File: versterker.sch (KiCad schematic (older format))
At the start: 0 parts

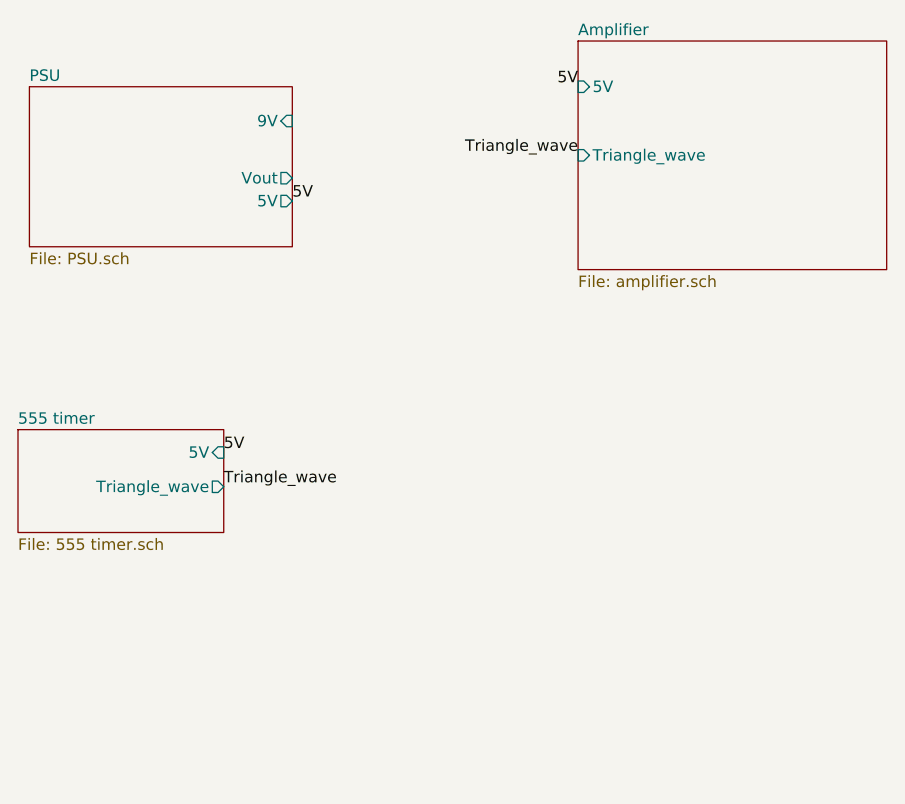
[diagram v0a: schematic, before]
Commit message: added filter end stage
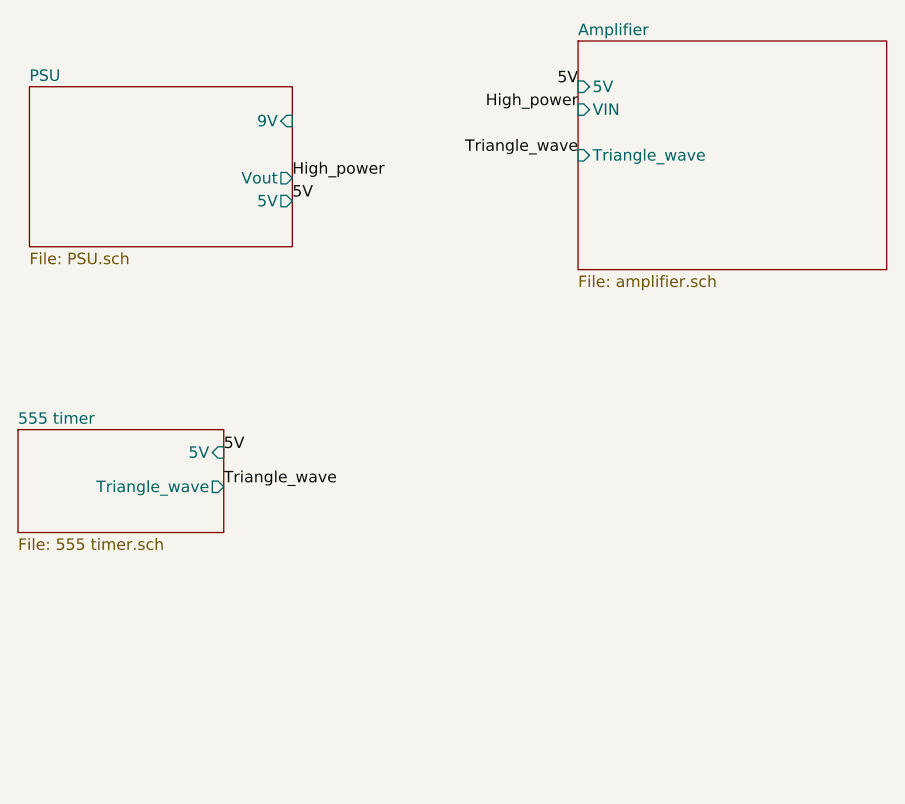
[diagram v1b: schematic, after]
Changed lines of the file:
@@
 F2 "5V" I L 3950 1600 50
 F3 "Triangle_wave" I L 3950 1900 50
+F4 "VIN" I L 3950 1700 50
 $EndSheet
 $Sheet
@@
 Text Label 3950 1600 2    50   ~ 0
 5V
+Text Label 2700 2000 0    50   ~ 0
+High_power
+Text Label 3950 1700 2    50   ~ 0
+High_power
 $EndSCHEMATC

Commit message: created pcb
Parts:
- added D1: D_SMCJ9.0CA_TVS, MAIN_PCB_LIB:D_9V_TVS_SMCJ-Q, symbol Main_Library:D_SMCJ9.0CA_TVS
- added D2: D_RED_0603_Wurth_150060RS75000, MAIN_PCB_LIB:D_RED_0603_Wurth, symbol Main_Library:D_RED_0603_Wurth_150060RS75000
- added J1: J_Barreljack_3.5mm_Wurth_TH, MAIN_PCB_LIB:J_Barreljack_3.5mm_Wurth, symbol Main_Library:J_Barreljack_3.5mm_Wurth_TH
- added R1: R_10K_0603, MAIN_PCB_LIB:R_0603, symbol Main_Library:R_10K_0603
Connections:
- new net: D2.1 (CATHODE), R1.1
- new net 9V: D1.1, D2.2 (ANODE), J1.1
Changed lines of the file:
@@
 $Descr A4 11693 8268
 encoding utf-8
-Sheet 1 4
+Sheet 1 5
 Title ""
 Date ""
@@
 $EndDescr
 $Sheet
-S 1550 1600 1150 700
+S 2150 1600 550  600
 U 615215B7
 F0 "PSU" 50
@@
 $EndSheet
 $Sheet
-S 3950 1400 1350 1000
+S 3950 1400 750  750
 U 6152C63E
 F0 "Amplifier" 50
@@
 $EndSheet
 $Sheet
-S 1500 3100 900  450
+S 2150 2550 900  450
 U 6158BEDE
 F0 "555 timer" 50
 F1 "555 timer.sch" 50
-F2 "5V" I R 2400 3200 50
-F3 "Triangle_wave" O R 2400 3350 50
+F2 "5V" I R 3050 2650 50
+F3 "Triangle_wave" O R 3050 2800 50
 $EndSheet
-Text Label 2400 3350 0    50   ~ 0
+Text Label 3050 2800 0    50   ~ 0
 Triangle_wave
 Text Label 3950 1900 2    50   ~ 0
@@
 Text Label 2700 2100 0    50   ~ 0
 5V
-Text Label 2400 3200 0    50   ~ 0
+Text Label 3050 2650 0    50   ~ 0
 5V
 Text Label 3950 1600 2    50   ~ 0
@@
 Text Label 3950 1700 2    50   ~ 0
 High_power
+$Sheet
+S 4100 2650 650  450
+U 616ED187
+F0 "VU-Meter" 50
+F1 "VU-Meter.sch" 50
+F2 "9V" I L 4100 2800 50
+F3 "Signal" I L 4100 2950 50
+$EndSheet
+Text Label 2700 1750 0    50   ~ 0
+9V
+Text Label 4100 2800 2    50   ~ 0
+9V
+Text Label 4100 2950 2    50   ~ 0
+High_power
+$Comp
+L Main_Library:J_Barreljack_3.5mm_Wurth_TH J1
+U 1 1 6176EC14
+P 2750 3750
+F 0 "J1" H 2570 3898 50  0000 C CNN
+F 1 "J_Barreljack_3.5mm_Wurth_TH" H 2350 3450 50  0001 L BNN
+F 2 "MAIN_PCB_LIB:J_Barreljack_3.5mm_Wurth" H 2750 3750 50  0001 L BNN
+F 3 "" H 2750 3750 50  0001 L BNN
+F 4 "710-694102303002" H 2750 3750 50  0001 C CNN "Mouser"
+	1    2750 3750
+	1    0    0    -1
+$EndComp
+Text Label 3500 3750 0    50   ~ 0
+9V
+$Comp
+L Main_Library:GND #GND01
+U 1 1 6177185F
+P 2900 3950
+F 0 "#GND01" H 2740 3930 50  0001 C CNN
+F 1 "GND" H 2740 3930 50  0001 C CNN
+F 2 "" H 2810 3890 50  0001 C CNN
+F 3 "" H 2810 3890 50  0001 C CNN
+	1    2900 3950
+	1    0    0    -1
+$EndComp
+Wire Wire Line
+	2750 3850 2900 3850
+Wire Wire Line
+	2900 3850 2900 3950
+$Comp
+L Main_Library:D_SMCJ9.0CA_TVS D1
+U 1 1 61776F94
+P 3100 4050
+F 0 "D1" V 3050 4130 50  0000 L CNN
+F 1 "D_SMCJ9.0CA_TVS" H 2800 3855 50  0001 L BNN
+F 2 "MAIN_PCB_LIB:D_9V_TVS_SMCJ-Q" H 3100 4050 50  0001 L BNN
+F 3 "" H 3100 4050 50  0001 L BNN
+F 4 "IPC-7351B" H 3100 4050 50  0001 L BNN "STANDARD"
+F 5 "Diodes Incorporated" H 3100 4050 50  0001 L BNN "MANUFACTURER"
+F 6 "2.62mm" H 3100 4050 50  0001 L BNN "MAXIMUM_PACKAGE_HEIGHT"
+F 7 "11/20/15" H 3100 4050 50  0001 L BNN "PARTREV"
+F 8 "576-SMCJ9.0CA" H 3100 4050 50  0001 C CNN "Mouser"
+	1    3100 4050
+	0    1    1    0
+$EndComp
+$Comp
+L Main_Library:GND #GND02
+U 1 1 617783BE
+P 3100 4250
+F 0 "#GND02" H 2940 4230 50  0001 C CNN
+F 1 "GND" H 2940 4230 50  0001 C CNN
+F 2 "" H 3010 4190 50  0001 C CNN
+F 3 "" H 3010 4190 50  0001 C CNN
+	1    3100 4250
+	1    0    0    -1
+$EndComp
+$Comp
+L Main_Library:D_RED_0603_Wurth_150060RS75000 D2
+U 1 1 617794CD
+P 3500 3700
+F 0 "D2" V 3846 3572 50  0000 R CNN
+F 1 "D_RED_0603_Wurth_150060RS75000" H 3500 4200 50  0001 L CNN
+F 2 "MAIN_PCB_LIB:D_RED_0603_Wurth" H 3500 4300 50  0001 L CNN
+F 3 "https://www.we-online.com/catalog/datasheet/150060RS75000.pdf" H 3500 4400 50  0001 L CNN
+F 4 "No" H 3500 4500 50  0001 L CNN "automotive"
+F 5 "Diode" H 3500 4600 50  0001 L CNN "category"
+F 6 "Red" V 3755 3572 50  0000 R CNN "colour"
+F 7 "Optoelectronics" H 3500 4800 50  0001 L CNN "device class L1"
+F 8 "LEDs" H 3500 4900 50  0001 L CNN "device class L2"
+F 9 "unset" H 3500 5000 50  0001 L CNN "device class L3"
+F 10 "LED RED CLEAR 0603 SMD" H 3500 5100 50  0001 L CNN "digikey description"
+F 11 "732-4978-1-ND" H 3500 5200 50  0001 L CNN "digikey part number"
+F 12 "20mA" H 3500 5300 50  0001 L CNN "forward current"
+F 13 "2V" H 3500 5400 50  0001 L CNN "forward voltage"
+F 14 "0.8mm" H 3500 5500 50  0001 L CNN "height"
+F 15 "Yes" H 3500 5600 50  0001 L CNN "lead free"
+F 16 "Top View" H 3500 5700 50  0001 L CNN "led orientation"
+F 17 "cd4e03a66a96d806" H 3500 5800 50  0001 L CNN "library id"
+F 18 "250mcd" H 3500 5900 50  0001 L CNN "luminous intensity"
+F 19 "Wurth" H 3500 6000 50  0001 L CNN "manufacturer"
+F 20 "+95°C" H 3500 6100 50  0001 L CNN "max junction temp"
+F 21 "Standard LEDs - SMD WL-SMCW SMDMono TpVw Waterclr 0603 Red" H 3500 6200 50  0001 L CNN "mouser description"
+F 22 "710-150060RS75000" H 3500 6300 50  0001 L CNN "mouser part number"
+F 23 "0603" H 3500 6400 50  0001 L CNN "package"
+F 24 "630nm" H 3500 6500 50  0001 L CNN "peak emmision wavelength"
+F 25 "72mW" H 3500 6600 50  0001 L CNN "power dissipation"
+F 26 "5V" H 3500 6700 50  0001 L CNN "reverse voltage"
+F 27 "Yes" H 3500 6800 50  0001 L CNN "rohs"
+F 28 "0mm" H 3500 6900 50  0001 L CNN "standoff height"
+F 29 "+85°C" H 3500 7000 50  0001 L CNN "temperature range high"
+F 30 "-40°C" H 3500 7100 50  0001 L CNN "temperature range low"
+F 31 "140°" H 3500 7200 50  0001 L CNN "viewing angle"
+F 32 "625nm" H 3500 7300 50  0001 L CNN "wavelength"
+	1    3500 3700
+	0    1    1    0
+$EndComp
+Wire Wire Line
+	3500 3750 3500 3800
+$Comp
+L Main_Library:GND #GND03
+U 1 1 61782307
+P 3500 4500
+F 0 "#GND03" H 3340 4480 50  0001 C CNN
+F 1 "GND" H 3340 4480 50  0001 C CNN
+F 2 "" H 3410 4440 50  0001 C CNN
+F 3 "" H 3410 4440 50  0001 C CNN
+	1    3500 4500
+	1    0    0    -1
+$EndComp
+Connection ~ 3100 3750
+Wire Wire Line
+	3100 3750 3500 3750
+Wire Wire Line
+	2750 3750 3100 3750
+$Comp
+L Main_Library:R_10K_0603 R1
+U 1 1 61785BEF
+P 3500 4350
+F 0 "R1" H 3553 4388 39  0000 L CNN
+F 1 "R_10K_0603" H 3450 4900 39  0001 C CNN
+F 2 "MAIN_PCB_LIB:R_0603" H 3500 4850 39  0001 C CNN
+F 3 "" H 3450 4500 39  0001 C CNN
+F 4 "10K" H 3553 4313 39  0000 L CNN "Waarde"
+F 5 "YAG1236CT-ND" H 3500 4950 39  0001 C CNN "Digi-key"
+	1    3500 4350
+	1    0    0    -1
+$EndComp
 $EndSCHEMATC

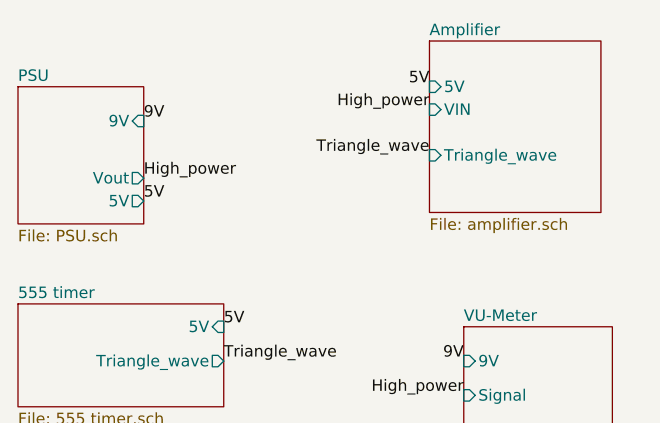
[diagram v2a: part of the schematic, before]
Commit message: added raspberry pi hat pcb outline and layout
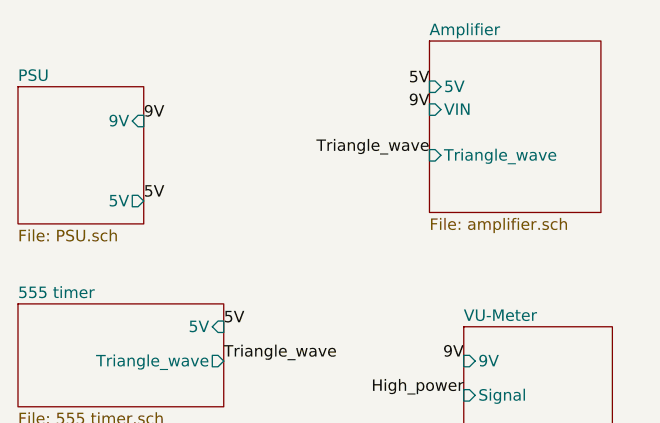
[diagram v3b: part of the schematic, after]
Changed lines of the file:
@@
 F1 "PSU.sch" 50
 F2 "9V" I R 2700 1750 50
-F3 "Vout" O R 2700 2000 50
-F4 "5V" O R 2700 2100 50
+F3 "5V" O R 2700 2100 50
 $EndSheet
 $Sheet
@@
 Text Label 3050 2650 0    50   ~ 0
 5V
-Text Label 3950 1600 2    50   ~ 0
-5V
-Text Label 2700 2000 0    50   ~ 0
-High_power
-Text Label 3950 1700 2    50   ~ 0
-High_power
 $Sheet
 S 4100 2650 650  450
@@
 	1    0    0    -1
 $EndComp
+Text Label 3950 1600 2    50   ~ 0
+5V
+Text Label 3950 1700 2    50   ~ 0
+9V
 $EndSCHEMATC

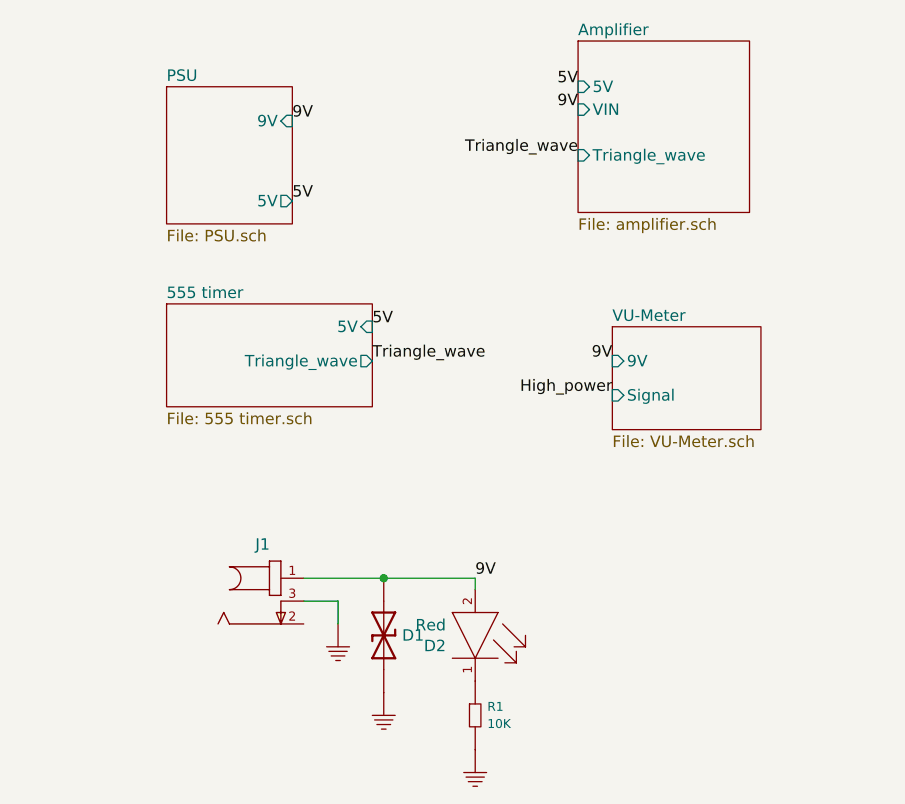
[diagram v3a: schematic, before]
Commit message: changed everything to 9V and changed inductor to match one in stock
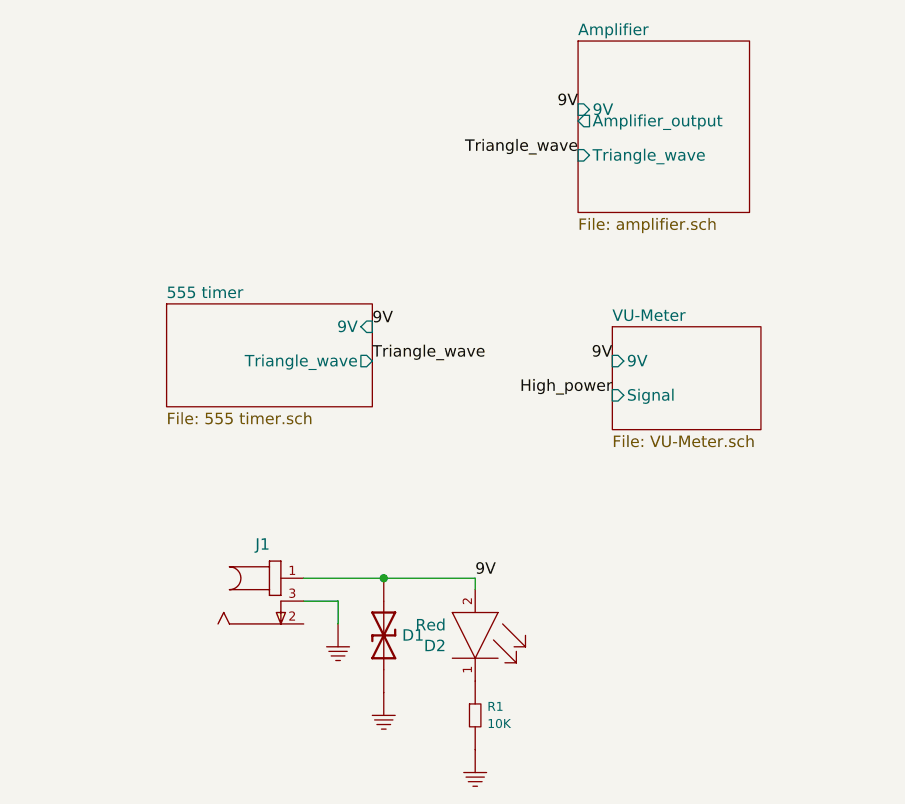
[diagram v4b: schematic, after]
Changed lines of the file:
@@
 $Descr A4 11693 8268
 encoding utf-8
-Sheet 1 5
+Sheet 1 4
 Title ""
 Date ""
@@
 $EndDescr
 $Sheet
-S 2150 1600 550  600
-U 615215B7
-F0 "PSU" 50
-F1 "PSU.sch" 50
-F2 "9V" I R 2700 1750 50
-F3 "5V" O R 2700 2100 50
-$EndSheet
-$Sheet
 S 3950 1400 750  750
 U 6152C63E
 F0 "Amplifier" 50
 F1 "amplifier.sch" 50
-F2 "5V" I L 3950 1600 50
-F3 "Triangle_wave" I L 3950 1900 50
-F4 "VIN" I L 3950 1700 50
+F2 "Triangle_wave" I L 3950 1900 50
+F3 "Amplifier_output" O L 3950 1750 50
+F4 "9V" I L 3950 1700 50
 $EndSheet
 $Sheet
@@
 F0 "555 timer" 50
 F1 "555 timer.sch" 50
-F2 "5V" I R 3050 2650 50
-F3 "Triangle_wave" O R 3050 2800 50
+F2 "Triangle_wave" O R 3050 2800 50
+F3 "9V" I R 3050 2650 50
 $EndSheet
 Text Label 3050 2800 0    50   ~ 0
@@
 Text Label 3950 1900 2    50   ~ 0
 Triangle_wave
-Text Label 2700 2100 0    50   ~ 0
-5V
-Text Label 3050 2650 0    50   ~ 0
-5V
 $Sheet
 S 4100 2650 650  450
@@
 F3 "Signal" I L 4100 2950 50
 $EndSheet
-Text Label 2700 1750 0    50   ~ 0
-9V
 Text Label 4100 2800 2    50   ~ 0
 9V
@@
 	1    0    0    -1
 $EndComp
-Text Label 3950 1600 2    50   ~ 0
-5V
 Text Label 3950 1700 2    50   ~ 0
 9V
+Text Label 3050 2650 0    50   ~ 0
+9V
 $EndSCHEMATC

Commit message: changed vu meter circuit
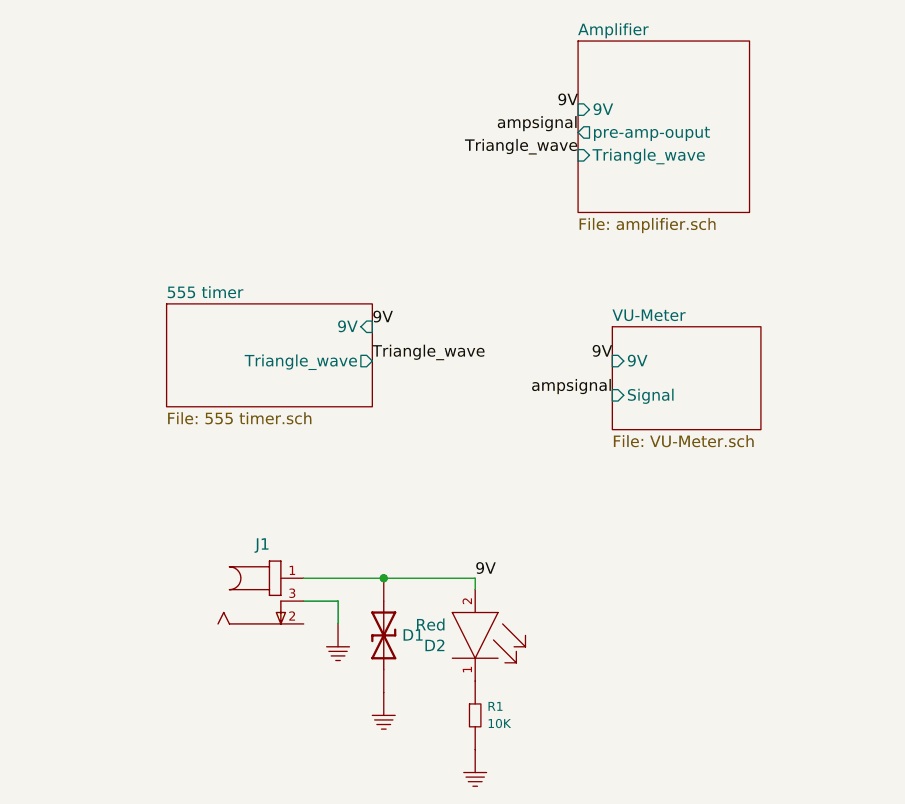
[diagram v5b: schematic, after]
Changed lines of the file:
@@
 F1 "amplifier.sch" 50
 F2 "Triangle_wave" I L 3950 1900 50
-F3 "Amplifier_output" O L 3950 1750 50
-F4 "9V" I L 3950 1700 50
+F3 "9V" I L 3950 1700 50
+F4 "pre-amp-ouput" O L 3950 1800 50
 $EndSheet
 $Sheet
@@
 Text Label 4100 2800 2    50   ~ 0
 9V
-Text Label 4100 2950 2    50   ~ 0
-High_power
 $Comp
 L Main_Library:J_Barreljack_3.5mm_Wurth_TH J1
@@
 Text Label 3050 2650 0    50   ~ 0
 9V
+Text Label 3950 1800 2    50   ~ 0
+ampsignal
+Text Label 4100 2950 2    50   ~ 0
+ampsignal
 $EndSCHEMATC
